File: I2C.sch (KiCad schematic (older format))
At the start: 18 parts, among them J201 1X4SMD-FPC, U201 OPT3001, U202 AT42QT1070-SSUR

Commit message: Last version before switching to resistive model to read the scroll wheel.
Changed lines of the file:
@@
 	4950 2550 4950 2450
-Wire Wire Line
-	6000 3050 5100 3050
 Wire Wire Line
 	4950 3050 4950 2550
@@
 Text HLabel 5100 1750 0    39   Input ~ 0
 TINT
-$Comp
-L power:PWR_FLAG #FLG0106
-U 1 1 5EB68594
-P 5100 2950
-F 0 "#FLG0106" H 5100 3025 50  0001 C CNN
-F 1 "PWR_FLAG" H 5100 3123 50  0000 C CNN
-F 2 "" H 5100 2950 50  0001 C CNN
-F 3 "~" H 5100 2950 50  0001 C CNN
-	1    5100 2950
-	1    0    0    -1
-$EndComp
-Wire Wire Line
-	5100 2950 5100 3050
-Connection ~ 5100 3050
-Wire Wire Line
-	5100 3050 4950 3050
 Text Label 7950 2150 3    39   ~ 0
 TGUARD
@@
 	0    -1   -1   0
 $EndComp
+Wire Wire Line
+	4950 3050 6000 3050
 $EndSCHEMATC

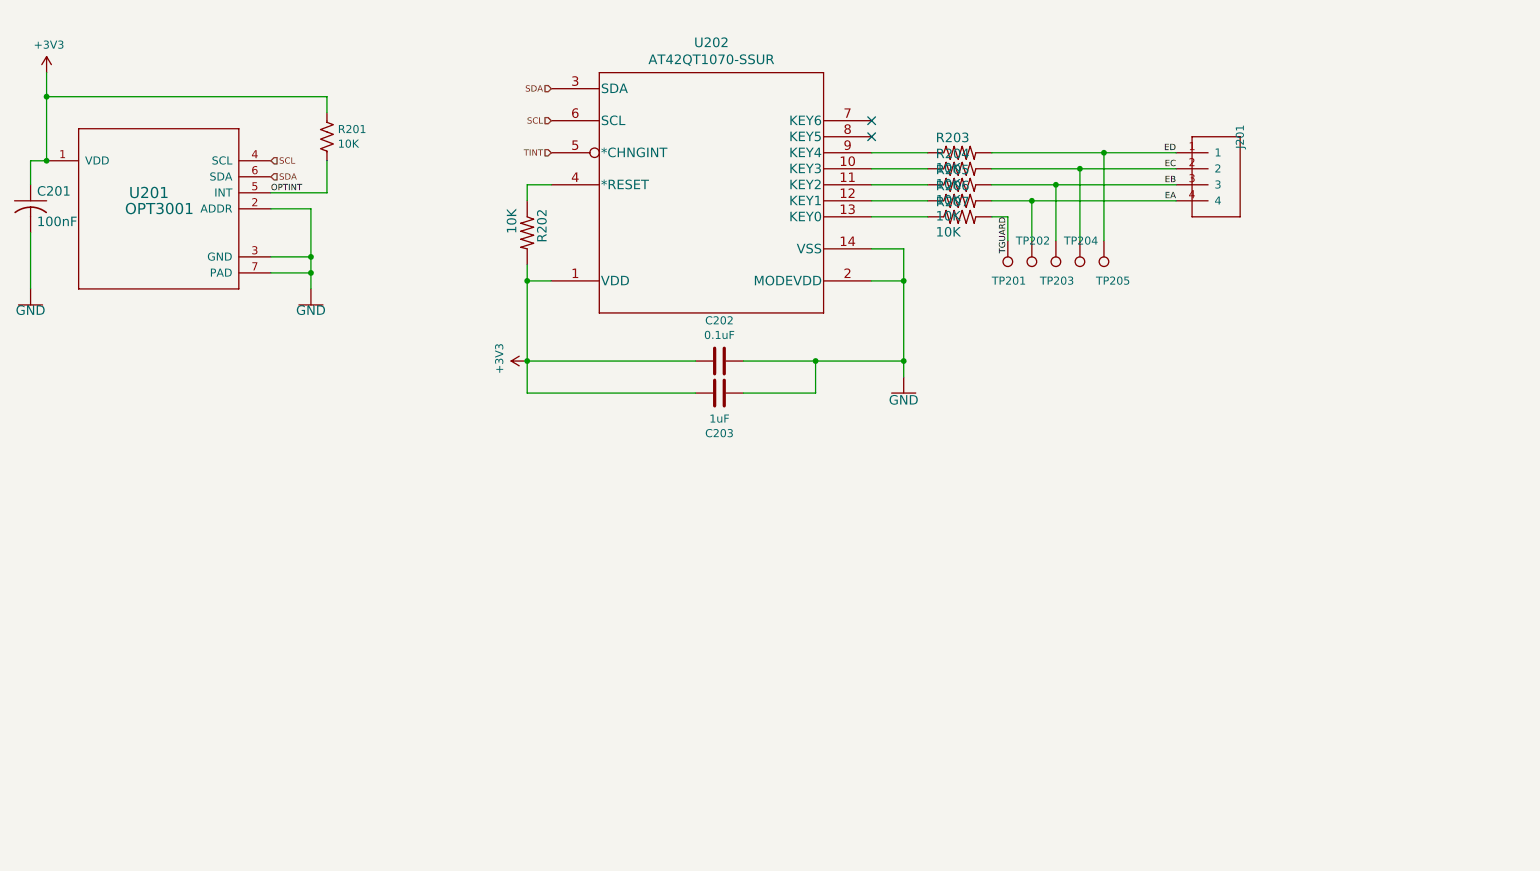
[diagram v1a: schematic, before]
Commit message: Version 2, DRC and ERC clear, ready to send, waiting on V1 to see what did not work.
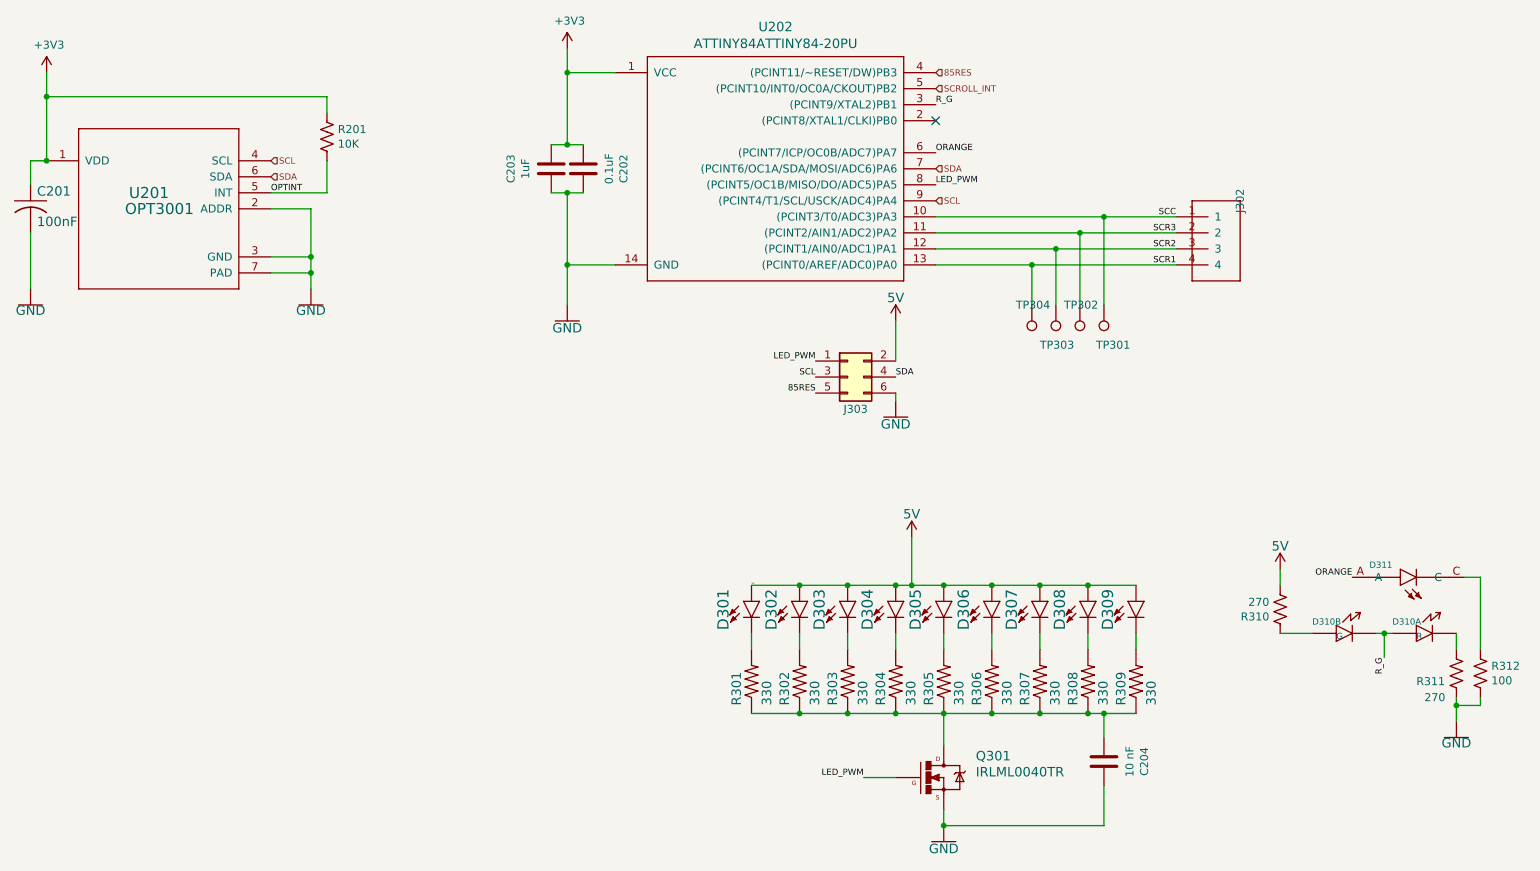
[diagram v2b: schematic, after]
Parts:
- removed J201: 1X4SMD-FPC, CPU:KYOCERA-6227-FPC_FFC, symbol CPU-eagle-import:1X4SMD-FPC
- removed R202, R203, R204, R205, R206, R207: 10K, Resistor_SMD:R_0805_2012Metric_Pad1.15x1.40mm_HandSolder, symbol CPU-eagle-import:R-US_R1206
- removed TP201, TP202, TP203, TP204, TP205: TestPoint, TestPoint:TestPoint_Pad_D1.0mm, symbol Connector:TestPoint
- removed U202: AT42QT1070-SSUR, UltraLibrarian:AT42QT1070-SSUR, symbol UltraLibrarian:AT42QT1070-I2C
- added C204: 10 nF, Capacitor_SMD:C_0805_2012Metric_Pad1.15x1.40mm_HandSolder, symbol Device:C
- added D301, D302, D303, D304, D305, D306, D307, D308, D309: LED0603, CPU:LED-0603, symbol CPU-eagle-import:LED0603
- added D310: RG, CPU:INOLUX_IN-S85DATRG, symbol CPU-eagle-import:DUAL_LEDINOLUX
- added D311: 598-8030-107F, CPU:LEDSC160X80X70L45N, symbol CPU-eagle-import:598-8030-107F
- added J302: 1X4SMD-FPC, CPU:KYOCERA-6227-FPC_FFC, symbol CPU-eagle-import:1X4SMD-FPC
- added J303: Conn_02x03_Odd_Even, Connector_PinHeader_2.54mm:PinHeader_2x03_P2.54mm_Vertical, symbol Connector_Generic:Conn_02x03_Odd_Even
- added Q301: IRLML0040TR, CPU:SOT23, symbol CPU-eagle-import:IRLML0040TR
- added R301, R302, R303, R304, R305, R306, R307, R308, R309: 330, CPU:R1206, symbol CPU-eagle-import:R-US_R1206
- added R310, R311: 270, Resistor_SMD:R_0805_2012Metric_Pad1.15x1.40mm_HandSolder, symbol Device:R_US
- added R312: 100, Resistor_SMD:R_0805_2012Metric_Pad1.15x1.40mm_HandSolder, symbol Device:R_US
- added TP301, TP302, TP303, TP304: TestPoint, TestPoint:TestPoint_Pad_D1.0mm, symbol Connector:TestPoint
- added U202: ATTINY84ATTINY84-20PU, MarcoK:14SOIC, symbol UltraLibrarian:ATTINY84ATTINY84-20PU
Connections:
- net +3V3: now also U202.1 (VCC)
- net SCL: now also J303.3 (Pin_3), U202.9 ((PCINT4/T1/SCL/USCK/ADC4)PA4)
- net SDA: now also J303.4 (Pin_4), U202.7 ((PCINT6/OC1A/SDA/MOSI/ADC6)PA6)
- net at C202.2, C203.1: now also U202.14 (GND)
- new net: D310.3 (K), R311.1
- new net: D310.2 (A), R310.1
- new net: D311.C, R312.1
- new net: R311.2, R312.2
- new net: D301.C, R301.2
- new net: C204.1, Q301.3 (D), R301.1, R302.1, R303.1, R304.1, R305.1, R306.1, R307.1, R308.1, R309.1
- new net: C204.2, Q301.2 (S)
- new net: D302.C, R302.2
- new net: D303.C, R303.2
- new net: D304.C, R304.2
- new net: D305.C, R305.2
- new net: D306.C, R306.2
- new net: D307.C, R307.2
- new net: D308.C, R308.2
- new net: D309.C, R309.2
- new net 5V: D301.A, D302.A, D303.A, D304.A, D305.A, D306.A, D307.A, D308.A, D309.A
- new net 85RES: J303.5 (Pin_5), U202.4 ((PCINT11/~~RESET/DW)PB3)
- new net LED_PWM: J303.1 (Pin_1), Q301.1 (G), U202.8 ((PCINT5/OC1B/MISO/DO/ADC5)PA5)
- new net ORANGE: D311.A, U202.6 ((PCINT7/ICP/OC0B/ADC7)PA7)
- new net R_G: D310.1 (K), D310.4 (A), U202.3 ((PCINT9/XTAL2)PB1)
- new net SCC: J302.1, TP301.1, U202.10 ((PCINT3/T0/ADC3)PA3)
- new net SCR1: J302.4, TP304.1, U202.13 ((PCINT0/AREF/ADC0)PA0)
- new net SCR2: J302.3, TP303.1, U202.12 ((PCINT1/AIN0/ADC1)PA1)
- new net SCR3: J302.2, TP302.1, U202.11 ((PCINT2/AIN1/ADC2)PA2)
- new net SCROLL_INT: U202.5 ((PCINT10/INT0/OC0A/CKOUT)PB2)
- no-connect marks 2 -> 1
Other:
- note added: "G"
- note added: "R"
- moved on the sheet: C202, C203
